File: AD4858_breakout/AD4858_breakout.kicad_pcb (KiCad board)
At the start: 4 copper layers, 140.2 x 140.2 mm, 184 parts, among them J1 142-0701-801, J10 142-0701-801, J11 142-0701-801, J12 142-0701-801, J13 142-0701-801, J14 142-0701-801, J15 142-0701-801, J16 142-0701-801, J17 Conn_01x02_Pin, J18 Conn_01x02_Pin, J19 Conn_01x02_Pin, J2 142-0701-801, J20 Conn_01x02_Pin, J21 Conn_01x02_Pin, J22 Conn_01x02_Pin, J23 Conn_01x02_Pin, J24 Conn_01x02_Pin, J25 Conn_01x02_Pin, J26 Conn_01x02_Pin, J27 Conn_01x02_Pin, J28 Conn_01x02_Pin, J29 Conn_01x02_Pin, J3 142-0701-801, J30 Conn_01x02_Pin, J31 Conn_01x02_Pin, J32 Conn_01x02_Pin, J33 Conn_01x02_Pin, J34 Conn_01x02_Pin, J35 Conn_01x02_Pin, J36 Conn_01x02_Pin, J37 Conn_01x02_Pin, J38 Conn_01x02_Pin, J39 Conn_01x02_Pin, J4 142-0701-801, J40 Conn_01x02_Pin, J41 Screw_Terminal_01x02, J42 Conn_01x02_Pin, J43 Conn_01x02_Pin, J44 Screw_Terminal_01x02, J45 Conn_01x02_Pin, J46 Conn_01x02_Pin, J47 Conn_01x02_Pin, J48 Conn_01x02_Pin, J49 Conn_01x02_Pin, J5 142-0701-801, J50 Conn_01x02_Pin, J51 Conn_01x02_Pin, J52 Conn_01x02_Pin, J53 Conn_01x02_Pin, J54 Conn_01x02_Pin, J55 Conn_01x02_Pin, J56 Conn_01x02_Pin, J57 Conn_01x02_Pin, J58 Conn_01x02_Pin, J59 Conn_01x02_Pin, J6 142-0701-801, J60 Conn_01x02_Pin, J61 Conn_01x02_Pin, J62 Conn_01x02_Pin, J63 Conn_01x02_Pin, J64 Conn_01x02_Pin, J65 Conn_01x02_Pin, J66 Conn_01x02_Pin, J67 Conn_01x02_Pin, J68 Conn_01x02_Pin, J69 Conn_01x02_Pin, J7 142-0701-801, J70 Conn_01x03_Pin, J71 Conn_01x03_Pin, J72 Conn_01x02_Pin, J73 Conn_01x03_Pin, J74 Conn_01x03_Pin, J8 142-0701-801, J9 142-0701-801, U1 AD4858BBCZ, U5 LT1761-5, U6 LT1761-SD, U7 LT1761-SD, U8 LT1761-SD

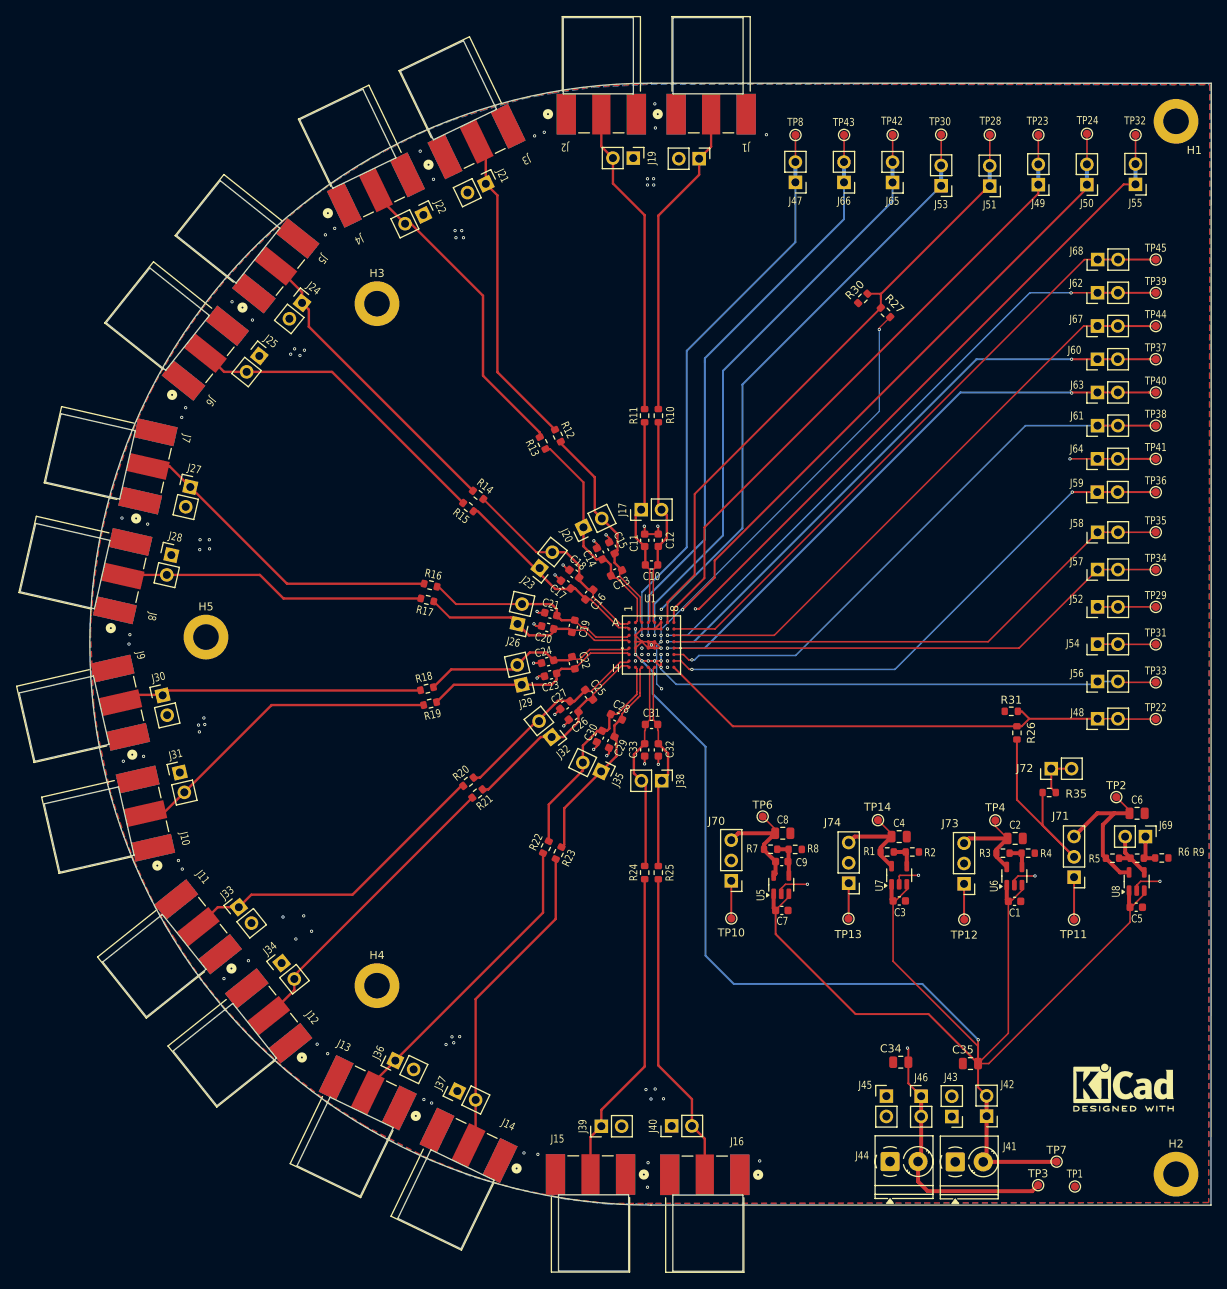
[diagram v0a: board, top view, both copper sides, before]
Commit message: Updated the PCB file with length matched SD_lines and stiched ground
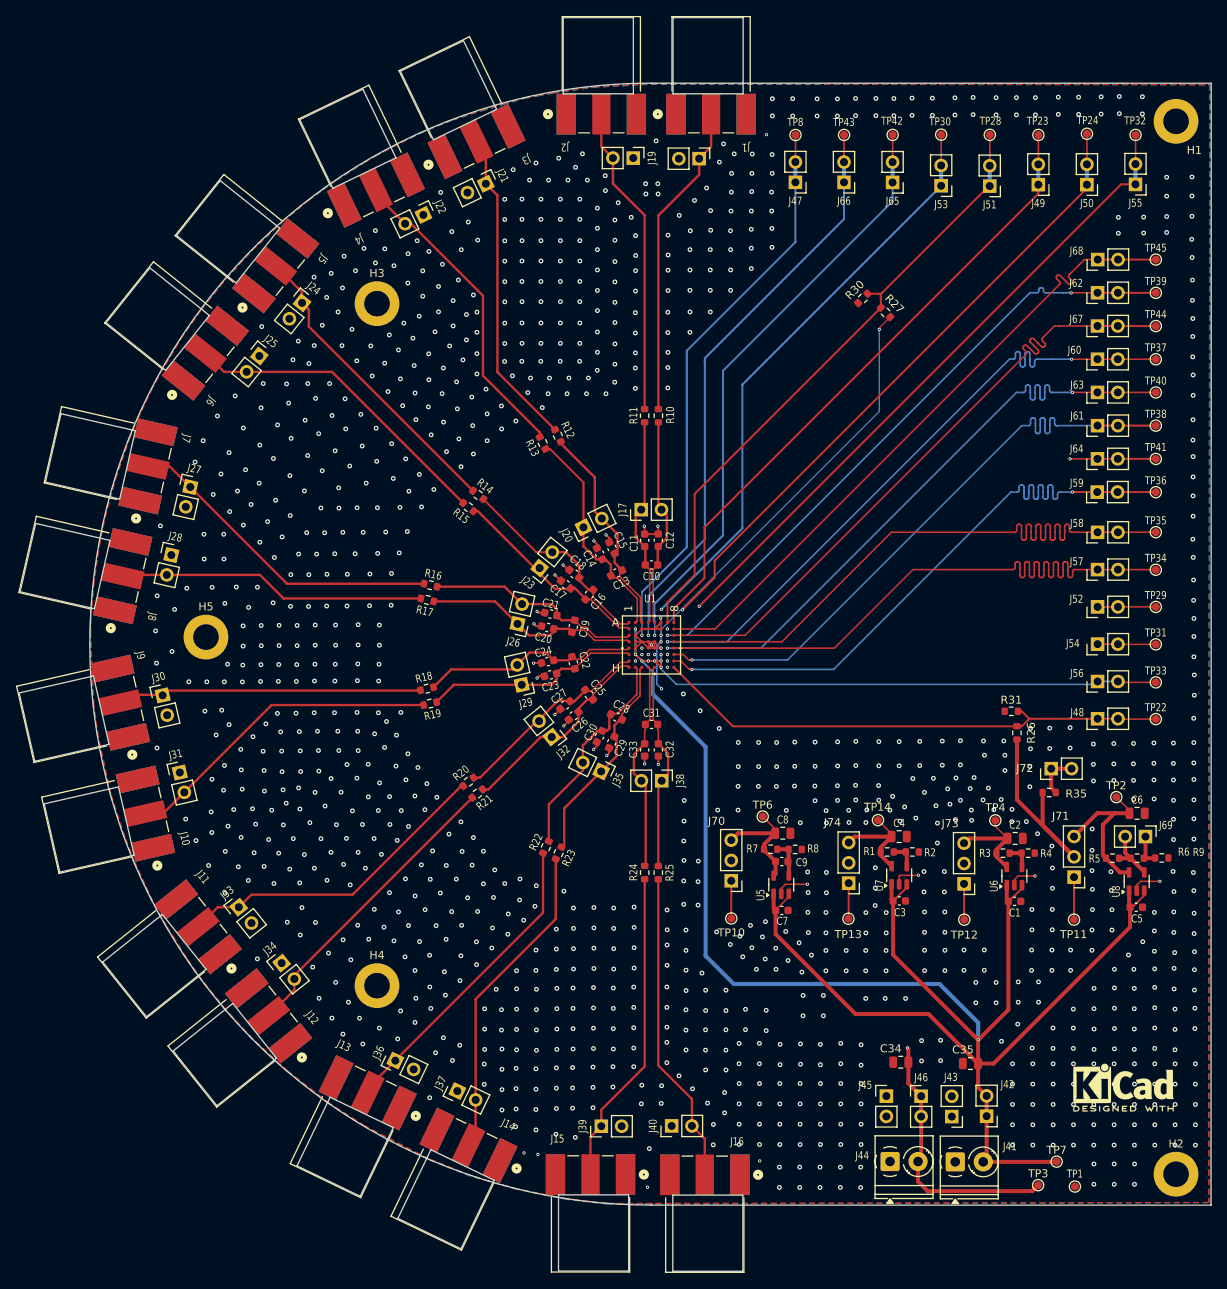
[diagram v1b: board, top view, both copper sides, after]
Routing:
- net /AD4858/SCKO-: track 64.3 -> 85.0 mm
- net /AD4858/SCKO+: track 65.9 -> 85.0 mm
- net /AD4858/CSCK: track 65.2 -> 83.6 mm
- net /AD4858/SDO7: track 69.9 -> 82.1 mm
- net /AD4858/SDO6: track 71.2 -> 82.3 mm
- net /AD4858/SDO5: track 72.6 -> 81.1 mm
- net /AD4858/SDO4: track 74.3 -> 82.1 mm
- net /AD4858/SDO3: track 75.7 -> 82.1 mm
- net /AD4858/SDO2: track 76.3 -> 82.7 mm
- net +12V: track 237.6 -> 233.1 mm
- net /AD4858/SDO0: track 79.4 -> 82.7 mm
- net /AD4858/1v8_VDDL: track 53.4 -> 55.6 mm
- net /AD4858/2v5_VDDH: track 40.9 -> 43.0 mm
- net /AD4858/5V_VDD: track 30.6 -> 32.3 mm
- net /AD4858/SDO1: track 78.8 -> 79.6 mm
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
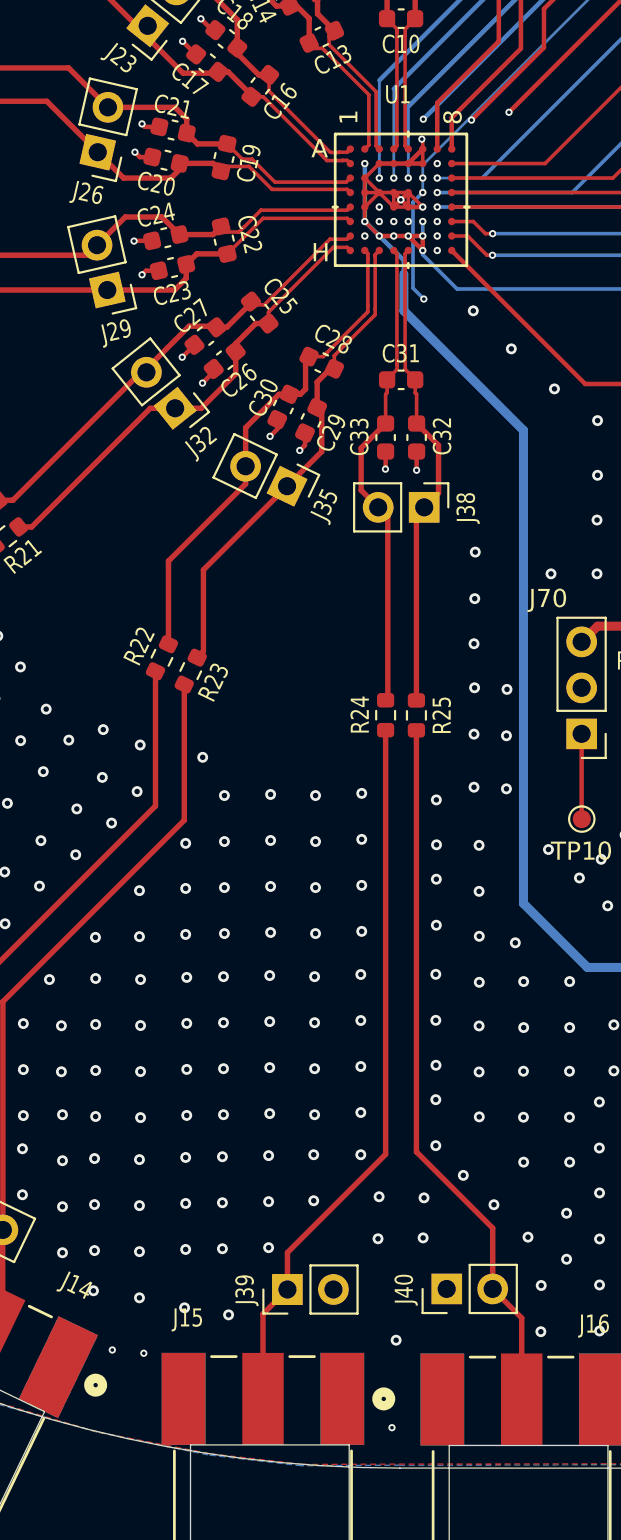
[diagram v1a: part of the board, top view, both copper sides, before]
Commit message: made all the vias to blind/buried which were missed out
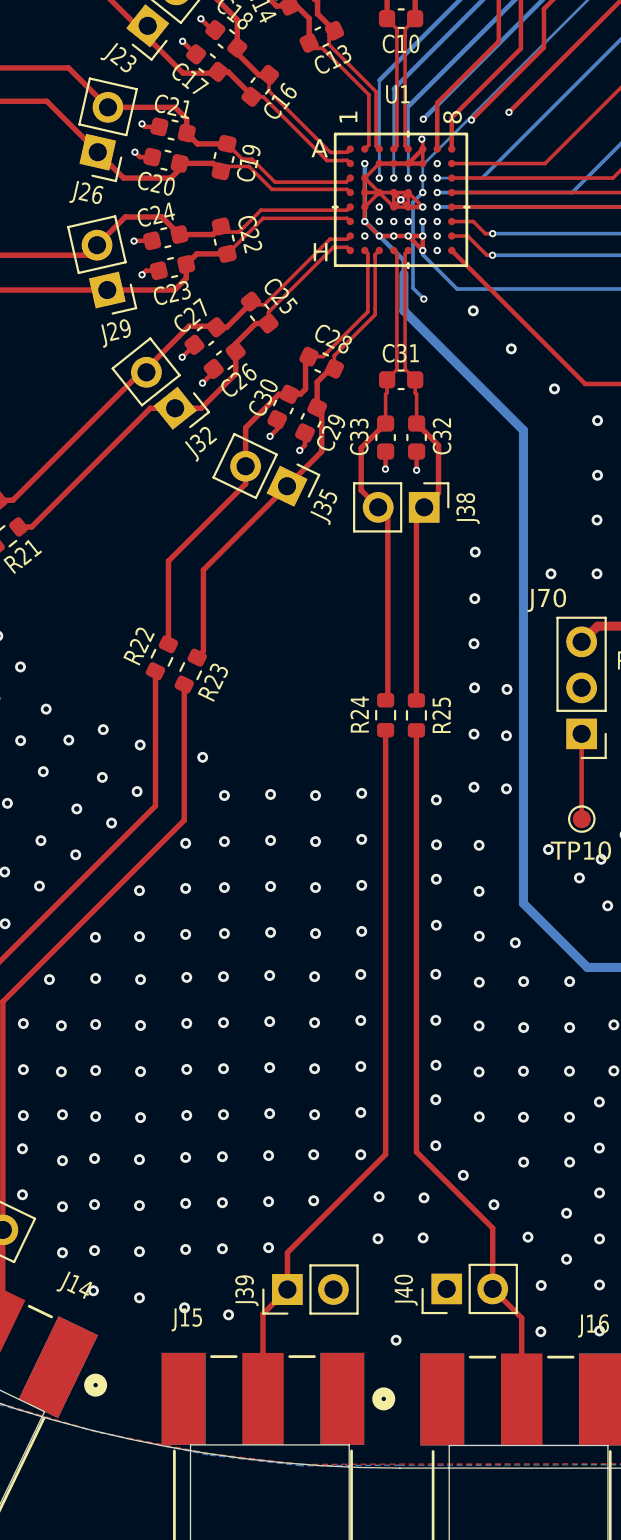
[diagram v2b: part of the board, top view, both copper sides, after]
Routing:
- net GND: vias 1174 -> 1171
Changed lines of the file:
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@@
 			(type default)
 		)
+		(locked yes)
 		(layer "Dwgs.User")
 	)
@@
 			(type solid)
 		)
+		(locked yes)
 		(layer "Dwgs.User")
 	)
@@
 			(type solid)
 		)
+		(locked yes)
 		(layer "Dwgs.User")
 	)
@@
 		(net 1)
 	)
-	(via
+	(via blind
 		(at 189.34 149.56)
 		(size 0.4)
@@
 		(net 1)
 	)
-	(via
+	(via blind
 		(at 146.5 98.2)
 		(size 0.4)
 		(drill 0.2)
 		(layers "F.Cu" "B.Cu")
-		(locked yes)
 		(net 1)
 	)
@@
 		(net 2)
 	)
-	(via
+	(via blind
 		(at 149.65 96.85)
 		(size 0.4)
@@
 	)
 	(via blind
-		(at 148 167.99)
-		(size 0.4)
-		(drill 0.2)
-		(layers "F.Cu" "B.Cu")
-		(remove_unused_layers yes)
-		(keep_end_layers no)
-		(free yes)
-		(zone_layer_connections "F.Cu" "In1.Cu" "In2.Cu" "B.Cu")
-		(net 2)
-	)
-	(via blind
 		(at 108.26 67.53)
 		(size 0.6)
@@
 	)
 	(via blind
-		(at 132.56 163.7)
-		(size 0.4)
-		(drill 0.2)
-		(layers "F.Cu" "B.Cu")
-		(remove_unused_layers yes)
-		(keep_end_layers no)
-		(free yes)
-		(zone_layer_connections "F.Cu" "In1.Cu" "In2.Cu" "B.Cu")
-		(net 2)
-	)
-	(via blind
 		(at 98.63 120.68)
 		(size 0.6)
@@
 		(net 2)
 	)
-	(via
+	(via blind
 		(at 148.49 100.2)
 		(size 0.4)
@@
 	)
 	(via blind
-		(at 134.3 163.88)
-		(size 0.4)
-		(drill 0.2)
-		(layers "F.Cu" "B.Cu")
-		(remove_unused_layers yes)
-		(keep_end_layers no)
-		(free yes)
-		(zone_layer_connections "F.Cu" "In1.Cu" "In2.Cu" "B.Cu")
-		(net 2)
-	)
-	(via blind
 		(at 127.96 71.32)
 		(size 0.6)
@@
 		(net 39)
 	)
-	(via
+	(via blind
 		(at 180.5 150.59)
 		(size 0.4)
@@
 		(net 45)
 	)
-	(via
+	(via blind
 		(at 150.5 102.2)
 		(size 0.4)
 		(drill 0.2)
-		(layers "F.Cu" "B.Cu")
+		(layers "F.Cu" "In2.Cu")
 		(remove_unused_layers yes)
 		(keep_end_layers no)
@@
 		(net 47)
 	)
-	(via
+	(via blind
 		(at 150.5 103)
 		(size 0.4)
 		(drill 0.2)
-		(layers "F.Cu" "B.Cu")
+		(layers "F.Cu" "In2.Cu")
 		(remove_unused_layers yes)
 		(keep_end_layers no)
@@
 		(net 48)
 	)
-	(via
+	(via blind
 		(at 150.5 98.2)
 		(size 0.4)
 		(drill 0.2)
-		(layers "F.Cu" "B.Cu")
+		(layers "F.Cu" "In2.Cu")
 		(remove_unused_layers yes)
 		(keep_end_layers no)
@@
 		(net 48)
 	)
-	(via
+	(via blind
 		(at 154.46 95.37)
 		(size 0.4)
 		(drill 0.2)
-		(layers "F.Cu" "B.Cu")
+		(layers "F.Cu" "In2.Cu")
 		(net 48)
 	)
@@
 		(net 49)
 	)
-	(via
+	(via blind
 		(at 149.7 101.4)
 		(size 0.4)
@@
 		(net 53)
 	)
-	(via
+	(via blind
 		(at 150.5 99.8)
 		(size 0.4)
@@
 		(net 55)
 	)
-	(via
+	(via blind
 		(at 150.5 99)
 		(size 0.4)
@@
 		(net 56)
 	)
-	(via
+	(via blind
 		(at 150.5 100.6)
 		(size 0.4)
@@
 		(net 57)
 	)
-	(via
+	(via blind
 		(at 150.5 101.4)
 		(size 0.4)
 		(drill 0.2)
-		(layers "F.Cu" "B.Cu")
+		(layers "F.Cu" "In2.Cu")
 		(remove_unused_layers yes)
 		(keep_end_layers no)
